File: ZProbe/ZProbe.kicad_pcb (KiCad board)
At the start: 2 copper layers, 23.5 x 13.5 mm, 10 parts, among them J1 SENSOR, J2 Vin, J3 Z-Probe, Q1 DTA124E, Q2 DTC124E

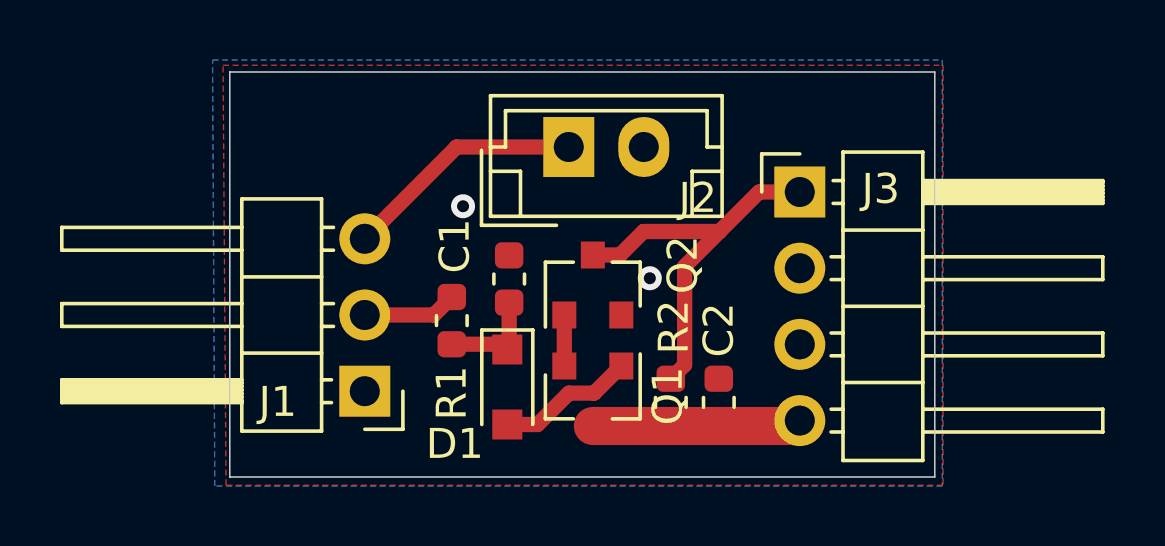
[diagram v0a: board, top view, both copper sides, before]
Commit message: Update ZProbe PCB labels. Make new gerbers.
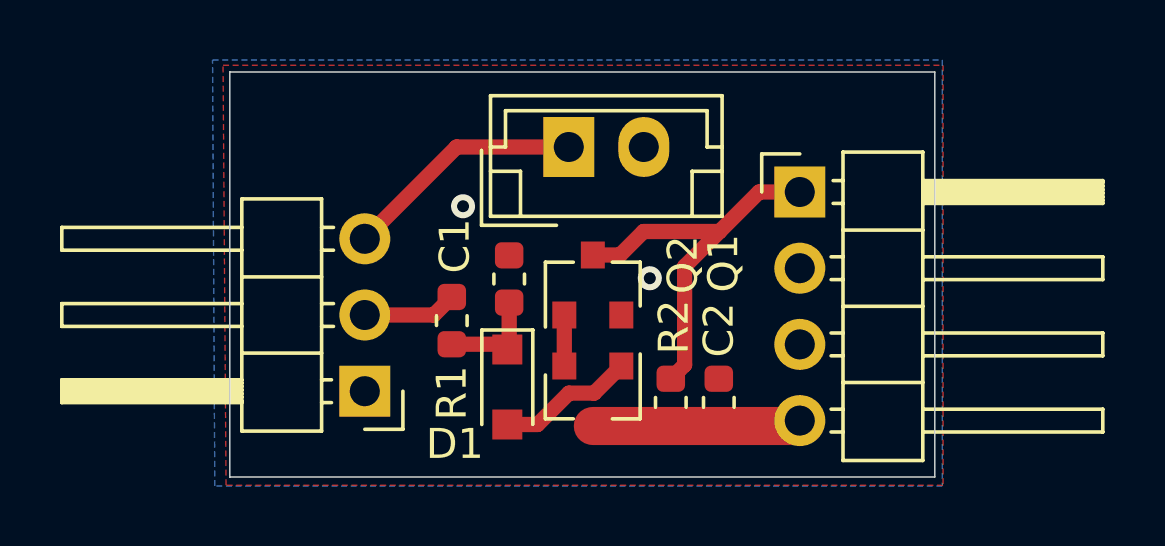
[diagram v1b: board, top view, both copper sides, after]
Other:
- board text added: "+ -"
- board text added: "5V"
- board text added: "GND"
- board text added: "In"
- board text added: "Out"
- board text added: "Pwr"
- board text added: "Vin"
- board text added: "n.c"
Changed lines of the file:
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@@
-(kicad_pcb (version 20171130) (host pcbnew 6.0.0-rc1-unknown-da35b16~65~ubuntu18.04.1)
+(kicad_pcb (version 20171130) (host pcbnew 6.0.0-rc1-unknown-6d2dfbb~65~ubuntu18.04.1)
   (general
     (thickness 1.6)
-    (drawings 4)
+    (drawings 13)
     (tracks 28)
     (zones 0)
@@
   (setup
     (last_trace_width 0.25)
-    (user_trace_width 0.1524)
     (user_trace_width 0.254)
     (user_trace_width 0.508)
@@
     (pcb_text_size 1.5 1.5)
     (mod_edge_width 0.12)
-    (mod_text_size 1 1)
-    (mod_text_width 0.15)
+    (mod_text_size 0.75 0.75)
+    (mod_text_width 0.1)
     (pad_size 1.524 1.524)
     (pad_drill 0.762)
@@
     (pcbplotparams
       (layerselection 0x010fc_ffffffff)
-      (usegerberextensions false)
+      (usegerberextensions true)
       (usegerberattributes false)
       (usegerberadvancedattributes false)
@@
     (descr "JST EH series connector, B02B-EH-A (http://www.jst-mfg.com/product/pdf/eng/eEH.pdf), generated with kicad-footprint-generator")
     (tags "connector JST EH side entry")
-    (fp_text reference J2 (at 4.3 1.7) (layer F.SilkS)
+    (fp_text reference J2 (at 4.3 1.7) (layer F.SilkS) hide
       (effects (font (size 1 1) (thickness 0.15)))
     )
@@
     (descr "Through hole angled pin header, 1x03, 2.54mm pitch, 6mm pin length, single row")
     (tags "Through hole angled pin header THT 1x03 2.54mm single row")
-    (fp_text reference J1 (at 2.9 -0.36 180) (layer F.SilkS)
+    (fp_text reference J1 (at 2.9 -0.36 180) (layer F.SilkS) hide
       (effects (font (size 1 1) (thickness 0.15)))
     )
@@
     (descr "Through hole angled pin header, 1x04, 2.54mm pitch, 6mm pin length, single row")
     (tags "Through hole angled pin header THT 1x04 2.54mm single row")
-    (fp_text reference J3 (at 2.7 -0.1) (layer F.SilkS)
+    (fp_text reference J3 (at 2.7 -0.1) (layer F.SilkS) hide
       (effects (font (size 1 1) (thickness 0.15)))
     )
@@
     (tags SOT-23)
     (attr smd)
-    (fp_text reference Q1 (at 0 -2.5 270) (layer F.SilkS)
+    (fp_text reference Q1 (at -4.425 -4.35 270) (layer F.SilkS)
       (effects (font (size 1 1) (thickness 0.15)))
     )
@@
     )
   )
+  (gr_text Vin (at 92.375 47.675) (layer B.SilkS)
+    (effects (font (size 0.75 0.75) (thickness 0.1)) (justify mirror))
+  )
+  (gr_text "+ -" (at 97.475 50.7 180) (layer B.SilkS)
+    (effects (font (size 1 1) (thickness 0.15)) (justify mirror))
+  )
+  (gr_text GND (at 86.875 56.75) (layer B.SilkS)
+    (effects (font (size 0.75 0.75) (thickness 0.1)) (justify mirror))
+  )
+  (gr_text In (at 87.275 54.05) (layer B.SilkS)
+    (effects (font (size 0.75 0.75) (thickness 0.1)) (justify mirror))
+  )
+  (gr_text Pwr (at 86.825 51.525) (layer B.SilkS)
+    (effects (font (size 0.75 0.75) (thickness 0.1)) (justify mirror))
+  )
+  (gr_text Out (at 106.7 49.95) (layer B.SilkS)
+    (effects (font (size 0.75 0.75) (thickness 0.1)) (justify mirror))
+  )
+  (gr_text GND (at 106.675 52.65) (layer B.SilkS)
+    (effects (font (size 0.75 0.75) (thickness 0.1)) (justify mirror))
+  )
+  (gr_text n.c (at 106.55 55) (layer B.SilkS)
+    (effects (font (size 0.75 0.75) (thickness 0.1)) (justify mirror))
+  )
+  (gr_text 5V (at 106.675 57.75) (layer B.SilkS)
+    (effects (font (size 0.75 0.75) (thickness 0.1)) (justify mirror))
+  )
   (gr_line (start 85 59.5) (end 85 46) (layer Edge.Cuts) (width 0.05))
